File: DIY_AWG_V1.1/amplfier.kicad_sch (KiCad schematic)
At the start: 20 parts, among them IC3 THS3091DDAR, IC5 LMH6505MAX, J3 Conn_Coaxial

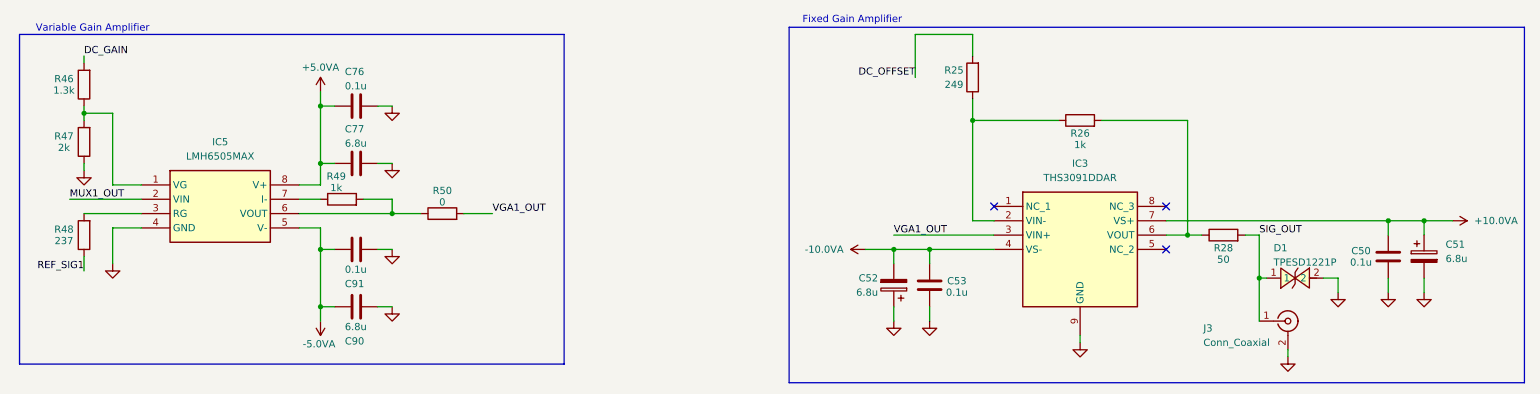
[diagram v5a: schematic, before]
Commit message: Updated AD9834_DDS, amplifier, STM32_MCU schematic
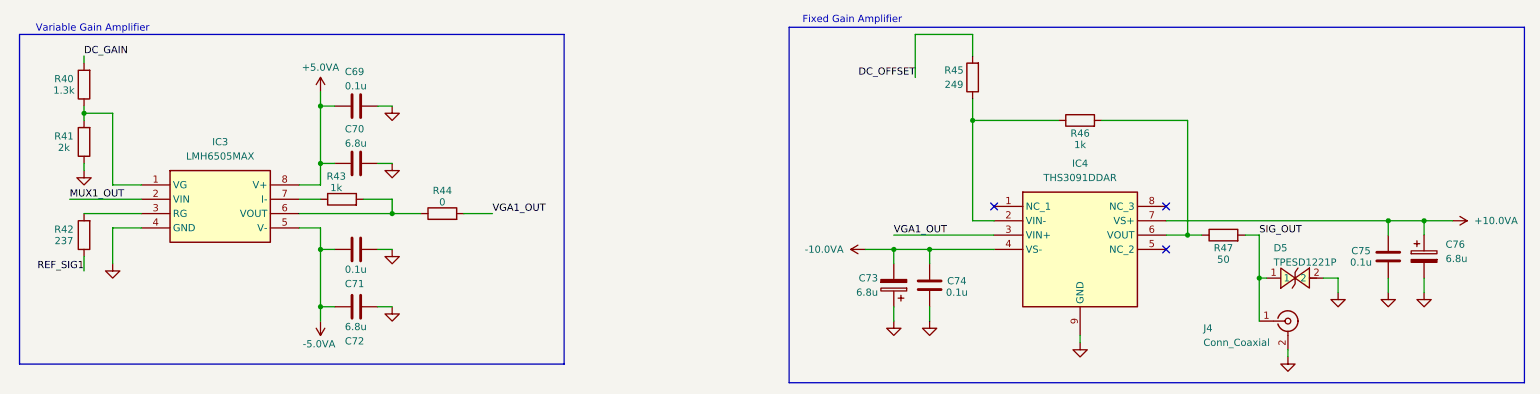
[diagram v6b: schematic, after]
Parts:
- renumbered C76 to C69, C77 to C70, C91 to C71, C90 to C72, C52 to C73, C53 to C74, C50 to C75, C51 to C76, D1 to D5, IC5 to IC3, IC3 to IC4, J3 to J4, R46 to R40, R47 to R41, R48 to R42, R49 to R43, R50 to R44, R25 to R45, R26 to R46, R28 to R47

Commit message: Updated power_supply, amplifier schematics
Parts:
- removed C73, C76: 6.8u, symbol Device:C_Polarized
- added C73, C76: 6.8u, symbol Device:C
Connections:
- net +10.0VA: now also C76.2
- net -10.0VA: now also C73.2
- net GND: now also C73.1, C76.1
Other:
- note added: "0.1uF MLCC (4): GCM188R71E224KA55D (4) 6.8uF MLCC (4): CL31A226KOHNNNE (4) 50 Resistor (1): RT0603BRD0750RL (1) 1k Resistor (1): THD03G1001BT (1)"
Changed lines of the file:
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@@
 		)
 	)
+	(text "0.1uF MLCC (4): GCM188R71E224KA55D (4)\n6.8uF MLCC (4): CL31A226KOHNNNE (4)\n\n50 Resistor (1): RT0603BRD0750RL (1)\n1k Resistor (1): THD03G1001BT (1)"
+		(exclude_from_sim no)
+		(at 20.574 84.074 0)
+		(effects
+			(font
+				(size 1.27 1.27)
+			)
+			(justify left)
+		)
+	)
 	(junction
 		(at 257.81 50.8)
@@
 	)
 	(symbol
-		(lib_id "Device:C_Polarized")
-		(at 170.18 62.23 180)
-		(unit 1)
-		(body_style 1)
-		(exclude_from_sim no)
-		(in_bom yes)
-		(on_board yes)
-		(in_pos_files yes)
-		(dnp no)
-		(property "Reference" "C73"
-			(at 167.386 60.96 0)
-			(show_name no)
-			(do_not_autoplace no)
-			(effects
-				(font
-					(size 1.27 1.27)
-				)
-				(justify left)
-			)
-		)
-		(property "Value" "6.8u"
-			(at 167.386 63.5 0)
-			(show_name no)
-			(do_not_autoplace no)
-			(effects
-				(font
-					(size 1.27 1.27)
-				)
-				(justify left)
-			)
-		)
-		(property "Footprint" ""
-			(at 169.2148 58.42 0)
-			(hide yes)
-			(show_name no)
-			(do_not_autoplace no)
-			(effects
-				(font
-					(size 1.27 1.27)
-				)
-			)
-		)
-		(property "Datasheet" ""
-			(at 170.18 62.23 0)
-			(hide yes)
-			(show_name no)
-			(do_not_autoplace no)
-			(effects
-				(font
-					(size 1.27 1.27)
-				)
-			)
-		)
-		(property "Description" "Polarized capacitor"
-			(at 170.18 62.23 0)
-			(hide yes)
-			(show_name no)
-			(do_not_autoplace no)
-			(effects
-				(font
-					(size 1.27 1.27)
-				)
-			)
-		)
-		(pin "2"
-		)
-		(pin "1"
-		)
-		(instances
-			(project "DIY_AWG_V1.1"
-				(path "/508078af-d961-4af3-840e-a064a9f8d5bc/faa0e7f2-4ad4-4392-8346-980541b6a840"
-					(reference "C73")
-					(unit 1)
-				)
-			)
-		)
-	)
-	(symbol
 		(lib_id "LMH6505MAX:LMH6505MAX")
 		(at 36.83 44.45 0)
@@
 	)
 	(symbol
-		(lib_id "Device:C_Polarized")
-		(at 264.16 57.15 0)
-		(unit 1)
-		(body_style 1)
-		(exclude_from_sim no)
-		(in_bom yes)
-		(on_board yes)
-		(in_pos_files yes)
-		(dnp no)
-		(fields_autoplaced yes)
-		(property "Reference" "C76"
-			(at 267.97 54.9909 0)
-			(show_name no)
-			(do_not_autoplace no)
-			(effects
-				(font
-					(size 1.27 1.27)
-				)
-				(justify left)
-			)
-		)
-		(property "Value" "6.8u"
-			(at 267.97 57.5309 0)
-			(show_name no)
-			(do_not_autoplace no)
-			(effects
-				(font
-					(size 1.27 1.27)
-				)
-				(justify left)
-			)
-		)
-		(property "Footprint" ""
-			(at 265.1252 60.96 0)
-			(hide yes)
-			(show_name no)
-			(do_not_autoplace no)
-			(effects
-				(font
-					(size 1.27 1.27)
-				)
-			)
-		)
-		(property "Datasheet" ""
-			(at 264.16 57.15 0)
-			(hide yes)
-			(show_name no)
-			(do_not_autoplace no)
-			(effects
-				(font
-					(size 1.27 1.27)
-				)
-			)
-		)
-		(property "Description" "Polarized capacitor"
-			(at 264.16 57.15 0)
-			(hide yes)
-			(show_name no)
-			(do_not_autoplace no)
-			(effects
-				(font
-					(size 1.27 1.27)
-				)
-			)
-		)
-		(pin "2"
-		)
-		(pin "1"
-		)
-		(instances
-			(project "DIY_AWG_V1.1"
-				(path "/508078af-d961-4af3-840e-a064a9f8d5bc/faa0e7f2-4ad4-4392-8346-980541b6a840"
-					(reference "C76")
-					(unit 1)
-				)
-			)
-		)
-	)
-	(symbol
 		(lib_id "Device:C")
 		(at 257.81 57.15 180)
@@
 	)
 	(symbol
+		(lib_id "Device:C")
+		(at 264.16 57.15 180)
+		(unit 1)
+		(body_style 1)
+		(exclude_from_sim no)
+		(in_bom yes)
+		(on_board yes)
+		(in_pos_files yes)
+		(dnp no)
+		(property "Reference" "C76"
+			(at 271.018 55.88 0)
+			(show_name no)
+			(do_not_autoplace no)
+			(effects
+				(font
+					(size 1.27 1.27)
+				)
+				(justify left)
+			)
+		)
+		(property "Value" "6.8u"
+			(at 271.018 58.42 0)
+			(show_name no)
+			(do_not_autoplace no)
+			(effects
+				(font
+					(size 1.27 1.27)
+				)
+				(justify left)
+			)
+		)
+		(property "Footprint" ""
+			(at 263.1948 53.34 0)
+			(hide yes)
+			(show_name no)
+			(do_not_autoplace no)
+			(effects
+				(font
+					(size 1.27 1.27)
+				)
+			)
+		)
+		(property "Datasheet" ""
+			(at 264.16 57.15 0)
+			(hide yes)
+			(show_name no)
+			(do_not_autoplace no)
+			(effects
+				(font
+					(size 1.27 1.27)
+				)
+			)
+		)
+		(property "Description" "Unpolarized capacitor"
+			(at 264.16 57.15 0)
+			(hide yes)
+			(show_name no)
+			(do_not_autoplace no)
+			(effects
+				(font
+					(size 1.27 1.27)
+				)
+			)
+		)
+		(pin "2"
+		)
+		(pin "1"
+		)
+		(instances
+			(project "DIY_AWG_V1.1"
+				(path "/508078af-d961-4af3-840e-a064a9f8d5bc/faa0e7f2-4ad4-4392-8346-980541b6a840"
+					(reference "C76")
+					(unit 1)
+				)
+			)
+		)
+	)
+	(symbol
 		(lib_id "power:+3.3VA")
 		(at 269.24 50.8 270)
@@
 					(unit 1)
 				)
+			)
+		)
+	)
+	(symbol
+		(lib_id "Device:C")
+		(at 170.18 62.23 0)
+		(mirror x)
+		(unit 1)
+		(body_style 1)
+		(exclude_from_sim no)
+		(in_bom yes)
+		(on_board yes)
+		(in_pos_files yes)
+		(dnp no)
+		(property "Reference" "C73"
+			(at 163.322 60.96 0)
+			(show_name no)
+			(do_not_autoplace no)
+			(effects
+				(font
+					(size 1.27 1.27)
+				)
+				(justify left)
+			)
+		)
+		(property "Value" "6.8u"
+			(at 163.322 63.5 0)
+			(show_name no)
+			(do_not_autoplace no)
+			(effects
+				(font
+					(size 1.27 1.27)
+				)
+				(justify left)
+			)
+		)
+		(property "Footprint" ""
+			(at 171.1452 58.42 0)
+			(hide yes)
+			(show_name no)
+			(do_not_autoplace no)
+			(effects
+				(font
+					(size 1.27 1.27)
+				)
+			)
+		)
+		(property "Datasheet" ""
+			(at 170.18 62.23 0)
+			(hide yes)
+			(show_name no)
+			(do_not_autoplace no)
+			(effects
+				(font
+					(size 1.27 1.27)
+				)
+			)
+		)
+		(property "Description" "Unpolarized capacitor"
+			(at 170.18 62.23 0)
+			(hide yes)
+			(show_name no)
+			(do_not_autoplace no)
+			(effects
+				(font
+					(size 1.27 1.27)
+				)
+			)
+		)
+		(pin "2"
+		)
+		(pin "1"
+		)
+		(instances
+			(project "DIY_AWG_V1.1"
+				(path "/508078af-d961-4af3-840e-a064a9f8d5bc/faa0e7f2-4ad4-4392-8346-980541b6a840"
+					(reference "C73")
+					(unit 1)
+				)

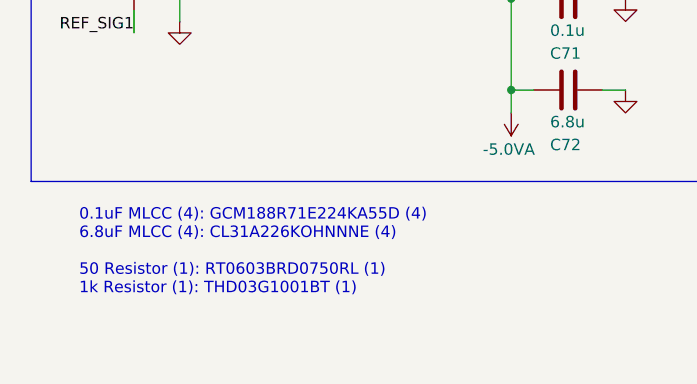
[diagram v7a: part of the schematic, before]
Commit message: Updated amplifier schematic
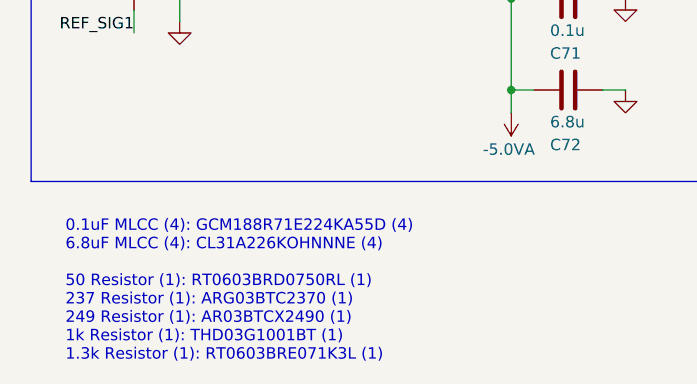
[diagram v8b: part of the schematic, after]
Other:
- note added: "0.1uF MLCC (4): GCM188R71E224KA55D (4) 6.8uF MLCC (4): CL31A226KOHNNNE (4) 50 Resistor (1): RT0603BRD0750RL (1) 237 Resistor (1): ARG03BTC2370 (1) 249 Resistor (1): AR03BTCX2490 (1) 1k Resistor (1): THD03G1001BT (1) 1.3k Resistor (1): RT0603BRE071K3L (1)"
- note removed: "0.1uF MLCC (4): GCM188R71E224KA55D (4) 6.8uF MLCC (4): CL31A226KOHNNNE (4) 50 Resistor (1): RT0603BRD0750RL (1) 1k Resistor (1): THD03G1001BT (1)"
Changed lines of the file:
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@@
 		)
 	)
-	(text "0.1uF MLCC (4): GCM188R71E224KA55D (4)\n6.8uF MLCC (4): CL31A226KOHNNNE (4)\n\n50 Resistor (1): RT0603BRD0750RL (1)\n1k Resistor (1): THD03G1001BT (1)"
+	(text "0.1uF MLCC (4): GCM188R71E224KA55D (4)\n6.8uF MLCC (4): CL31A226KOHNNNE (4)\n\n50 Resistor (1): RT0603BRD0750RL (1)\n237 Resistor (1): ARG03BTC2370 (1)\n249 Resistor (1): AR03BTCX2490 (1)\n1k Resistor (1): THD03G1001BT (1)\n1.3k Resistor (1): RT0603BRE071K3L (1)"
 		(exclude_from_sim no)
-		(at 20.574 84.074 0)
+		(at 19.05 88.392 0)
 		(effects
 			(font
